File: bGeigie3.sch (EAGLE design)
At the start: 103 parts, among them Q1 FDN360P, Q2 16MHz, Q3 8MHz, Q4 8MHz, Q5 FDN360P, Q6 FDN360P, Q7 FDN360P

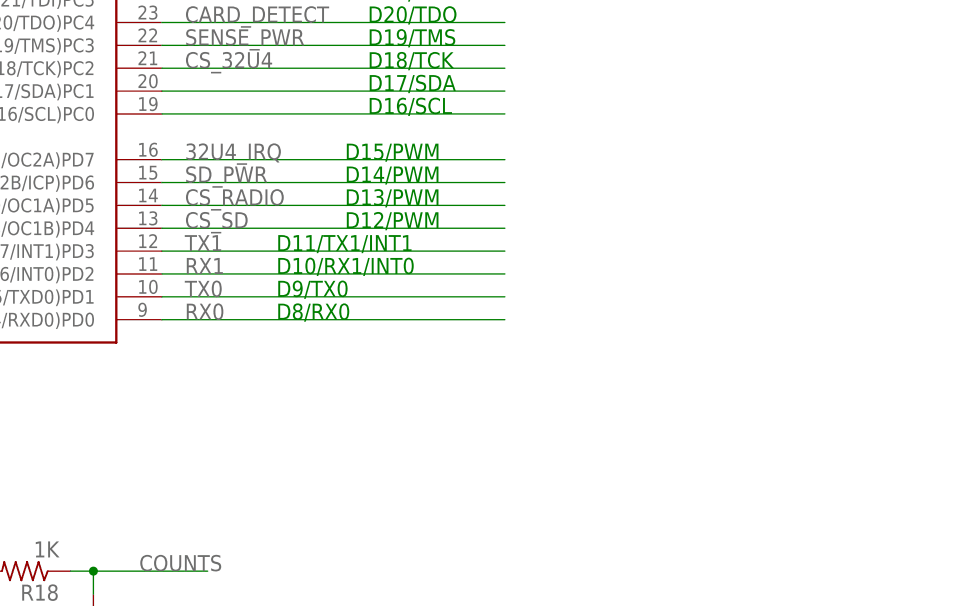
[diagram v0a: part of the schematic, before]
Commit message: Added serial header for debugging.
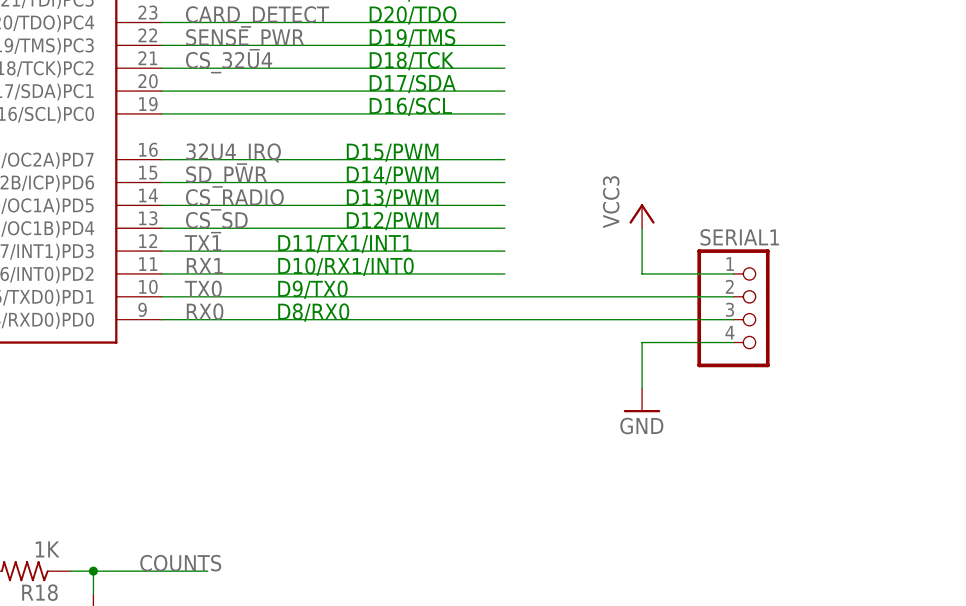
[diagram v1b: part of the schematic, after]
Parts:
- added SERIAL1: (no value), pinhead:PINHD-1X4
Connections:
- net GND: now also SERIAL1.4
- net RX0: now also SERIAL1.3
- net TX0: now also SERIAL1.2
- net VCC3: now also SERIAL1.1
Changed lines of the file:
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@@
 <part name="VCC14" library="supply1" deviceset="VCC" device="" value="VCC3"/>
 <part name="GND51" library="supply1" deviceset="GND" device=""/>
+<part name="SERIAL1" library="pinhead" deviceset="PINHD-1X4" device=""/>
+<part name="P+9" library="supply1" deviceset="VCC" device="" value="VCC3"/>
+<part name="GND28" library="supply1" deviceset="GND" device=""/>
 </parts>
 <sheets>
@@
 <instance part="VCC14" gate="VCC" x="86.36" y="22.86"/>
 <instance part="GND51" gate="1" x="86.36" y="0"/>
+<instance part="SERIAL1" gate="A" x="378.46" y="-43.18"/>
+<instance part="P+9" gate="VCC" x="365.76" y="-30.48"/>
+<instance part="GND28" gate="1" x="365.76" y="-53.34"/>
 </instances>
 <busses>
@@
 <pinref part="GND51" gate="1" pin="GND"/>
 </segment>
+<segment>
+<pinref part="SERIAL1" gate="A" pin="4"/>
+<pinref part="GND28" gate="1" pin="GND"/>
+<wire x1="375.92" y1="-45.72" x2="365.76" y2="-45.72" width="0.1524" layer="91"/>
+<wire x1="365.76" y1="-45.72" x2="365.76" y2="-50.8" width="0.1524" layer="91"/>
+</segment>
 </net>
 <net name="VBATT" class="0">
@@
 <pinref part="C37" gate="G$1" pin="+"/>
 </segment>
+<segment>
+<pinref part="SERIAL1" gate="A" pin="1"/>
+<pinref part="P+9" gate="VCC" pin="VCC"/>
+<wire x1="375.92" y1="-38.1" x2="365.76" y2="-38.1" width="0.1524" layer="91"/>
+<wire x1="365.76" y1="-38.1" x2="365.76" y2="-33.02" width="0.1524" layer="91"/>
+</segment>
 </net>
 <net name="N$6" class="0">
@@
 <net name="RX0" class="0">
 <segment>
-<wire x1="312.42" y1="-43.18" x2="350.52" y2="-43.18" width="0.1524" layer="91"/>
+<wire x1="312.42" y1="-43.18" x2="375.92" y2="-43.18" width="0.1524" layer="91"/>
 <label x="314.96" y="-43.18" size="1.778" layer="95"/>
 <pinref part="1284P" gate="G$1" pin="(PCINT24/RXD0)PD0"/>
+<pinref part="SERIAL1" gate="A" pin="3"/>
 </segment>
 <segment>
@@
 <net name="TX0" class="0">
 <segment>
-<wire x1="312.42" y1="-40.64" x2="350.52" y2="-40.64" width="0.1524" layer="91"/>
-<label x="314.96" y="-40.64" size="1.778" layer="95"/>
-<pinref part="1284P" gate="G$1" pin="(PCINT25/TXD0)PD1"/>
-</segment>
-<segment>
 <wire x1="71.12" y1="-187.96" x2="78.74" y2="-187.96" width="0.1524" layer="91"/>
 <label x="76.2" y="-187.96" size="1.778" layer="95"/>
 <pinref part="32U4" gate="G$1" pin="PD2(INT2/RXD1)"/>
 </segment>
-</net>
+<segment>
+<pinref part="1284P" gate="G$1" pin="(PCINT25/TXD0)PD1"/>
+<pinref part="SERIAL1" gate="A" pin="2"/>
+<wire x1="312.42" y1="-40.64" x2="375.92" y2="-40.64" width="0.1524" layer="91"/>
+<label x="314.96" y="-40.64" size="1.778" layer="95"/>
+</segment>
+</net>
